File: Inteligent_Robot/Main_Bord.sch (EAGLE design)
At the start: 88 parts, among them CN5 DF11-4DS-2C, CN6 DF11-4DS-2C, CN7 IL-G_ST_4, CN8 IL-G_ST_4, IC1 TWE-001L-IP, IC2 LTC2862A, IC5 A4988, IC7 A4988

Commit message: Refime pisitions
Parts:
- added 0R1, 0R2: 5106, Keystone:5106
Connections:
- new net N$10: 0R2.2, CN1.3
- new net N$11: 0R1.2, CN1.2
- net N$1: now also 0R2.1; no longer CN1.2
- net N$2: now also 0R1.1; no longer CN1.3
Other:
- moved on the sheet: CN1
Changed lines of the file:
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@@
 <layer number="59" name="tCarbon" color="7" fill="1" visible="no" active="no"/>
 <layer number="60" name="bCarbon" color="7" fill="1" visible="no" active="no"/>
+<layer number="88" name="SimResults" color="9" fill="1" visible="yes" active="yes"/>
+<layer number="89" name="SimProbes" color="9" fill="1" visible="yes" active="yes"/>
 <layer number="90" name="Modules" color="5" fill="1" visible="yes" active="yes"/>
 <layer number="91" name="Nets" color="2" fill="1" visible="yes" active="yes"/>
@@
 <part name="C10" library="Murata" deviceset="GMR31" device=""/>
 <part name="GND8" library="supply1" library_urn="urn:adsk.eagle:library:371" deviceset="GND" device=""/>
+<part name="0R1" library="Keystone" deviceset="5106" device=""/>
+<part name="0R2" library="Keystone" deviceset="5106" device=""/>
 </parts>
 <sheets>
@@
 <instance part="KIT1" gate="KIT" x="40.64" y="60.96"/>
 <instance part="IC1" gate="G$1" x="218.44" y="53.34" rot="MR0"/>
-<instance part="CN1" gate="G$1" x="60.96" y="7.62" rot="R180"/>
+<instance part="CN1" gate="G$1" x="50.8" y="7.62" rot="R180"/>
 <instance part="CN3" gate="G$1" x="43.18" y="-99.06"/>
 <instance part="GND2" gate="1" x="243.84" y="-25.4" rot="MR0"/>
@@
 <instance part="+3.3V1" gate="G$1" x="-43.18" y="142.24"/>
 <instance part="GND5" gate="1" x="185.42" y="20.32" rot="MR0"/>
-<instance part="P+2" gate="VCC" x="76.2" y="27.94"/>
-<instance part="GND6" gate="1" x="68.58" y="27.94" rot="MR180"/>
+<instance part="P+2" gate="VCC" x="66.04" y="27.94"/>
+<instance part="GND6" gate="1" x="58.42" y="27.94" rot="MR180"/>
 <instance part="P+5" gate="VCC" x="-10.16" y="-17.78"/>
 <instance part="GND11" gate="1" x="-15.24" y="-53.34"/>
@@
 <instance part="C10" gate="G$1" x="193.04" y="-114.3"/>
 <instance part="GND8" gate="1" x="-12.7" y="76.2"/>
+<instance part="0R1" gate="G$1" x="73.66" y="5.08"/>
+<instance part="0R2" gate="G$1" x="86.36" y="7.62"/>
 </instances>
 <busses>
@@
 <segment>
 <pinref part="CN1" gate="G$1" pin="5"/>
-<wire x1="60.96" y1="12.7" x2="68.58" y2="12.7" width="0.1524" layer="91"/>
+<wire x1="50.8" y1="12.7" x2="58.42" y2="12.7" width="0.1524" layer="91"/>
 <pinref part="GND6" gate="1" pin="GND"/>
-<wire x1="68.58" y1="12.7" x2="68.58" y2="25.4" width="0.1524" layer="91"/>
+<wire x1="58.42" y1="12.7" x2="58.42" y2="25.4" width="0.1524" layer="91"/>
 </segment>
 <segment>
@@
 <segment>
 <pinref part="CN1" gate="G$1" pin="1"/>
-<wire x1="60.96" y1="2.54" x2="76.2" y2="2.54" width="0.1524" layer="91"/>
+<wire x1="50.8" y1="2.54" x2="66.04" y2="2.54" width="0.1524" layer="91"/>
 <pinref part="P+2" gate="VCC" pin="VCC"/>
-<wire x1="76.2" y1="2.54" x2="76.2" y2="25.4" width="0.1524" layer="91"/>
+<wire x1="66.04" y1="2.54" x2="66.04" y2="25.4" width="0.1524" layer="91"/>
 </segment>
 <segment>
@@
 <pinref part="KIT1" gate="KIT" pin="P21"/>
 <wire x1="88.9" y1="35.56" x2="93.98" y2="35.56" width="0.1524" layer="91"/>
-<wire x1="93.98" y1="35.56" x2="93.98" y2="5.08" width="0.1524" layer="91"/>
-<pinref part="CN1" gate="G$1" pin="2"/>
-<wire x1="60.96" y1="5.08" x2="93.98" y2="5.08" width="0.1524" layer="91"/>
-<junction x="93.98" y="5.08"/>
+<wire x1="93.98" y1="35.56" x2="93.98" y2="7.62" width="0.1524" layer="91"/>
 <pinref part="RA2" gate="-3" pin="1"/>
-<wire x1="93.98" y1="0" x2="93.98" y2="5.08" width="0.1524" layer="91"/>
+<pinref part="0R2" gate="G$1" pin="1"/>
+<wire x1="93.98" y1="7.62" x2="93.98" y2="0" width="0.1524" layer="91"/>
+<wire x1="91.44" y1="7.62" x2="93.98" y2="7.62" width="0.1524" layer="91"/>
+<junction x="93.98" y="7.62"/>
 </segment>
 </net>
@@
 <pinref part="KIT1" gate="KIT" pin="P22"/>
 <wire x1="88.9" y1="38.1" x2="99.06" y2="38.1" width="0.1524" layer="91"/>
-<wire x1="99.06" y1="38.1" x2="99.06" y2="7.62" width="0.1524" layer="91"/>
-<pinref part="CN1" gate="G$1" pin="3"/>
-<wire x1="99.06" y1="7.62" x2="99.06" y2="-7.62" width="0.1524" layer="91"/>
-<wire x1="60.96" y1="7.62" x2="99.06" y2="7.62" width="0.1524" layer="91"/>
-<junction x="99.06" y="7.62"/>
+<wire x1="99.06" y1="38.1" x2="99.06" y2="5.08" width="0.1524" layer="91"/>
 <pinref part="RA2" gate="-4" pin="1"/>
+<pinref part="0R1" gate="G$1" pin="1"/>
+<wire x1="99.06" y1="5.08" x2="99.06" y2="-7.62" width="0.1524" layer="91"/>
+<wire x1="78.74" y1="5.08" x2="99.06" y2="5.08" width="0.1524" layer="91"/>
+<junction x="99.06" y="5.08"/>
 </segment>
 </net>
@@
 <segment>
 <pinref part="CN1" gate="G$1" pin="4"/>
-<wire x1="60.96" y1="10.16" x2="88.9" y2="10.16" width="0.1524" layer="91"/>
+<wire x1="50.8" y1="10.16" x2="88.9" y2="10.16" width="0.1524" layer="91"/>
 <label x="78.74" y="10.16" size="1.778" layer="95"/>
 </segment>
@@
 </segment>
 </net>
+<net name="N$10" class="0">
+<segment>
+<pinref part="0R2" gate="G$1" pin="2"/>
+<pinref part="CN1" gate="G$1" pin="3"/>
+<wire x1="50.8" y1="7.62" x2="81.28" y2="7.62" width="0.1524" layer="91"/>
+</segment>
+</net>
+<net name="N$11" class="0">
+<segment>
+<pinref part="0R1" gate="G$1" pin="2"/>
+<pinref part="CN1" gate="G$1" pin="2"/>
+<wire x1="50.8" y1="5.08" x2="68.58" y2="5.08" width="0.1524" layer="91"/>
+</segment>
+</net>

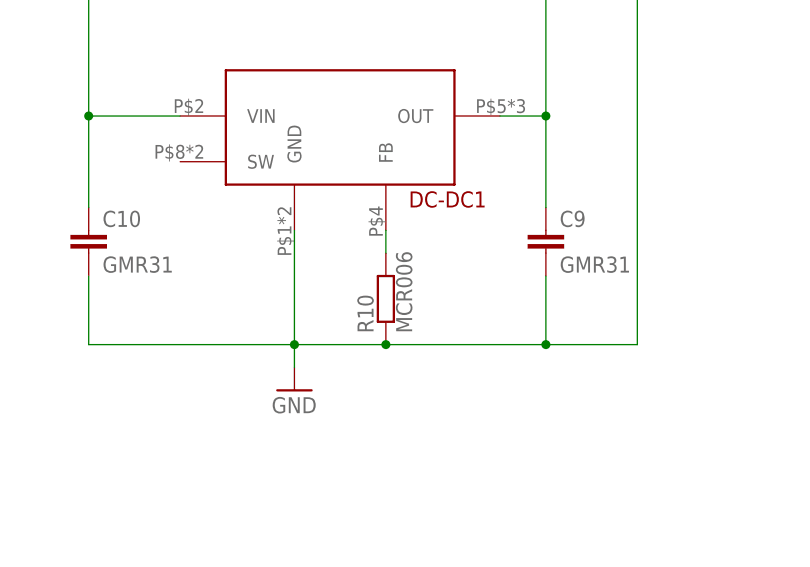
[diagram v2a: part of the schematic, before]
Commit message: Add Groung  solid pattern
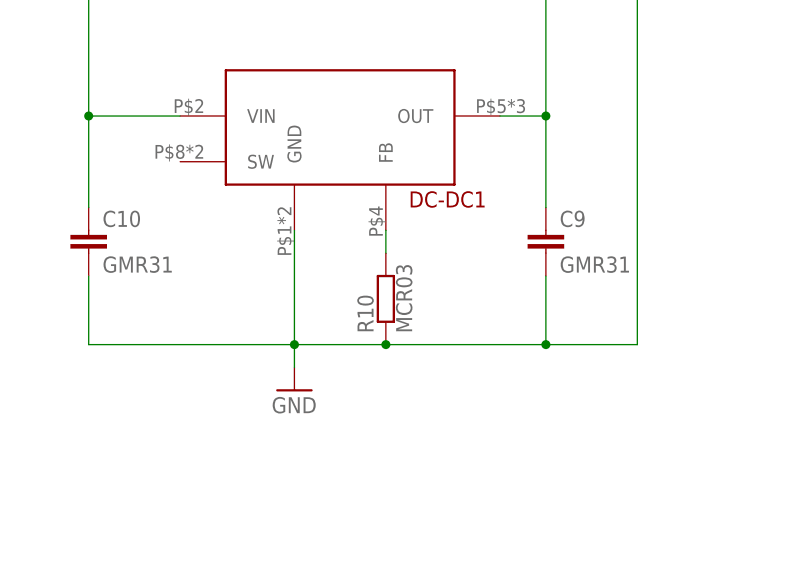
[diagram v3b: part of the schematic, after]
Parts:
- R10: value MCR006 -> MCR03; device ROHM:MCR006 -> ROHM:MCR03
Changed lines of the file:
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@@
 <part name="C9" library="Murata" deviceset="GMR31" device=""/>
 <part name="DC13" library="TDK" deviceset="YFF21PC" device=""/>
-<part name="R10" library="ROHM" deviceset="MCR006" device=""/>
+<part name="R10" library="ROHM" deviceset="MCR03" device=""/>
 <part name="C10" library="Murata" deviceset="GMR31" device=""/>
 <part name="GND8" library="supply1" library_urn="urn:adsk.eagle:library:371" deviceset="GND" device=""/>
